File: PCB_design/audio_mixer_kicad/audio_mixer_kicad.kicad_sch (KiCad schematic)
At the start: 0 parts

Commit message: Schematics v1
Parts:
- added D1, D2: SS34, symbol Device:D_Schottky_Small
- added J1, J10, J11, J12, J13, J14, J15, J16, J17, J18, J19, J2, J20, J21, J22, J23, J24, J25, J26, J27, J28, J29, J3, J30, J31, J32, J33, J34, J35, J36, J4, J5, J6, J7, J8, J9: B3B-XH-AMLFSN, CONN_B3B-XH-AMLFSN_JST, symbol JST_XH:B3B-XH-AMLFSN
- added J37: Screw_Terminal_01x02, symbol Connector:Screw_Terminal_01x02
- added R1, R2, R3, R4, R6: 4.7k, symbol Device:R_Small_US
- added R5: 0, symbol Device:R_Small_US
- added TP1: GND, symbol Connector:TestPoint
- added TP10: D3, symbol Connector:TestPoint
- added TP11: D4, symbol Connector:TestPoint
- added TP12: D5, symbol Connector:TestPoint
- added TP13: D6, symbol Connector:TestPoint
- added TP14: D7, symbol Connector:TestPoint
- added TP15: D8, symbol Connector:TestPoint
- added TP16: D9, symbol Connector:TestPoint
- added TP17: D10, symbol Connector:TestPoint
- added TP18: D11, symbol Connector:TestPoint
- added TP19: D12, symbol Connector:TestPoint
- added TP2: 5V, symbol Connector:TestPoint
- added TP20: D13, symbol Connector:TestPoint
- added TP21: D14, symbol Connector:TestPoint
- added TP22: A15, symbol Connector:TestPoint
- added TP23: A16, symbol Connector:TestPoint
- added TP24: D17, symbol Connector:TestPoint
- added TP25: D18, symbol Connector:TestPoint
- added TP26: D19, symbol Connector:TestPoint
- added TP27: D20, symbol Connector:TestPoint
- added TP28: D21, symbol Connector:TestPoint
- added TP29: D22, symbol Connector:TestPoint
- added TP3: 3.3VD, symbol Connector:TestPoint
- added TP30: D23, symbol Connector:TestPoint
- added TP31: RST_N, symbol Connector:TestPoint
- added TP32: FPGA_CS, symbol Connector:TestPoint
- added TP33: I2C1_SDA, symbol Connector:TestPoint
- added TP34: I2C1_SCL, symbol Connector:TestPoint
- added TP35: I2C0_SDA, symbol Connector:TestPoint
- added TP36: I2C0_SCL, symbol Connector:TestPoint
- added TP37: TX, symbol Connector:TestPoint
- added TP38: D48, symbol Connector:TestPoint
- added TP39: D47, symbol Connector:TestPoint
- added TP4: 3.3VA, symbol Connector:TestPoint
- added TP40: D46, symbol Connector:TestPoint
- added TP41: D45, symbol Connector:TestPoint
- added TP42: D44, symbol Connector:TestPoint
- added TP43: D43, symbol Connector:TestPoint
- added TP44: D42, symbol Connector:TestPoint
- added TP45: D41, symbol Connector:TestPoint
- added TP46: D40, symbol Connector:TestPoint
- added TP47: D39, symbol Connector:TestPoint
- added TP48: D38, symbol Connector:TestPoint
- added TP49: D37, symbol Connector:TestPoint
- added TP5: 48V, symbol Connector:TestPoint
- added TP50: D36, symbol Connector:TestPoint
- added TP51: D35, symbol Connector:TestPoint
- added TP52: D34, symbol Connector:TestPoint
- added TP53: D33, symbol Connector:TestPoint
- added TP54: D32, symbol Connector:TestPoint
- added TP55: D31, symbol Connector:TestPoint
- added TP56: D30, symbol Connector:TestPoint
- added TP57: D29, symbol Connector:TestPoint
- added TP58: D28, symbol Connector:TestPoint
- added TP59: D27, symbol Connector:TestPoint
- added TP6: +15V, symbol Connector:TestPoint
- added TP60: D26, symbol Connector:TestPoint
- added TP61: 3V3, symbol Connector:TestPoint
- added TP62: MOSI, symbol Connector:TestPoint
- added TP63: MISO, symbol Connector:TestPoint
- added TP64: SCK, symbol Connector:TestPoint
- added TP65: RX, symbol Connector:TestPoint
- added TP66: GPO1_0, symbol Connector:TestPoint
- added TP67: GPIO1_0, symbol Connector:TestPoint
- added TP68: GPIO2_0, symbol Connector:TestPoint
- added TP69: GPO1_1, symbol Connector:TestPoint
- added TP7: -15V, symbol Connector:TestPoint
- added TP70: GPIO1_1, symbol Connector:TestPoint
- added TP71: GPIO2_1, symbol Connector:TestPoint
- added TP8: D1, symbol Connector:TestPoint
- added TP9: D2, symbol Connector:TestPoint
- added U1: XIAO-ESP32-S3-DIP, Seeed_Studio_XIAO_Series:XIAO-ESP32-S3-DIP, symbol XIAO_symbols:XIAO-ESP32-S3-DIP
- added U2: Cmod A7-35T, symbol audio_mixer_symbols:Cmod_A7-35T
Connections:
- new net: TP21.1, U2.14 (D14)
- new net: TP52.1, U2.34 (D34)
- new net: TP19.1, U2.12 (D12)
- new net: TP20.1, U2.13 (D13)
- new net: TP51.1, U2.35 (D35)
- new net: TP48.1, U2.38 (D38)
- new net: TP22.1, U2.15 (A15)
- new net: TP23.1, U2.16 (A16)
- new net: TP24.1, U2.17 (D17)
- new net: TP25.1, U2.18 (D18)
- new net: D1.1 (K), U2.24 (VU)
- new net: TP58.1, U2.28 (D28)
- new net: TP57.1, U2.29 (D29)
- new net: TP56.1, U2.30 (D30)
- new net: TP55.1, U2.31 (D31)
- new net: TP54.1, U2.32 (D32)
- new net: TP53.1, U2.33 (D33)
- new net: TP50.1, U2.36 (D36)
- new net: TP49.1, U2.37 (D37)
- new net: TP47.1, U2.39 (D39)
- new net: TP46.1, U2.40 (D40)
- new net: TP45.1, U2.41 (D41)
- new net: TP44.1, U2.42 (D42)
- new net: TP43.1, U2.43 (D43)
- new net: TP42.1, U2.44 (D44)
- new net: TP41.1, U2.45 (D45)
- new net: TP40.1, U2.46 (D46)
- new net: D2.1 (K), U1.14 (VBUS)
- new net: TP61.1, U1.12 (3V3)
- new net +15V: TP6.1
- new net +3.3V: R1.1, R2.1, R3.1, R4.1, TP3.1
- new net +3.3VA: TP4.1
- new net +48V: TP5.1
- new net +5V: D1.2 (A), D2.2 (A), TP2.1
- new net -15V: TP7.1
- new net A_PWRGATE: TP60.1, U2.26 (D26)
- new net A_PWRGATE2: TP59.1, U2.27 (D27)
- new net BCLK: TP10.1, U2.3 (D3)
- new net CH10_XLR+: J10.2
- new net CH10_XLR-: J10.3
- new net CH11_XLR+: J11.2
- new net CH11_XLR-: J11.3
- new net CH12_XLR+: J12.2
- new net CH12_XLR-: J12.3
- new net CH13_XLR+: J13.2
- new net CH13_XLR-: J13.3
- new net CH14_XLR+: J14.2
- new net CH14_XLR-: J14.3
- new net CH15_XLR+: J15.2
- new net CH15_XLR-: J15.3
- new net CH16_XLR+: J16.2
- new net CH16_XLR-: J16.3
- new net CH17_XLR+: J17.2
- new net CH17_XLR-: J17.3
- new net CH18_XLR+: J18.2
- new net CH18_XLR-: J18.3
- new net CH19_XLR+: J19.2
- new net CH19_XLR-: J19.3
- new net CH1_XLR+: J1.2
- new net CH1_XLR-: J1.3
- new net CH20_XLR+: J20.2
- new net CH20_XLR-: J20.3
- new net CH21_XLR+: J21.2
- new net CH21_XLR-: J21.3
- new net CH22_XLR+: J22.2
- new net CH22_XLR-: J22.3
- new net CH23_XLR+: J23.2
- new net CH23_XLR-: J23.3
- new net CH24_XLR+: J24.2
- new net CH24_XLR-: J24.3
- new net CH25_XLR+: J25.2
- new net CH25_XLR-: J25.3
- new net CH26_XLR+: J26.2
- new net CH26_XLR-: J26.3
- new net CH27_XLR+: J27.2
- new net CH27_XLR-: J27.3
- new net CH28_XLR+: J28.2
- new net CH28_XLR-: J28.3
- new net CH29_XLR+: J29.2
- new net CH29_XLR-: J29.3
- new net CH2_XLR+: J2.2
- new net CH2_XLR-: J2.3
- new net CH30_XLR+: J30.2
- new net CH30_XLR-: J30.3
- new net CH31_XLR+: J31.2
- new net CH31_XLR-: J31.3
- new net CH32_XLR+: J32.2
- new net CH32_XLR-: J32.3
- new net CH3_XLR+: J3.2
- new net CH3_XLR-: J3.3
- new net CH4_XLR+: J4.2
- new net CH4_XLR-: J4.3
- new net CH5_XLR+: J5.2
- new net CH5_XLR-: J5.3
- new net CH6_XLR+: J6.2
- new net CH6_XLR-: J6.3
- new net CH7_XLR+: J7.2
- new net CH7_XLR-: J7.3
- new net CH8_XLR+: J8.2
- new net CH8_XLR-: J8.3
- new net CH9_XLR+: J9.2
- new net CH9_XLR-: J9.3
- new net DAC0/ADDR: R5.1
- new net DAC0/GPIO1: TP67.1
- new net DAC0/GPIO2: TP68.1
- new net DAC0/GPO1: TP66.1
- new net DAC1/ADDR: R6.1
- new net DAC1/GPIO1: TP70.1
- new net DAC1/GPIO2: TP71.1
- new net DAC1/GPO1: TP69.1
- new net DIN0: TP38.1, U2.48 (D48)
- new net DIN1: TP39.1, U2.47 (D47)
- new net FPGA_CS: TP27.1, TP32.1, U1.2 (GPIO2_A1_D1), U2.20 (D20)
- new net FSYNC: TP9.1, U2.2 (D2)
- new net GND: J1.1, J10.1, J11.1, J12.1, J13.1, J14.1, J15.1, J16.1, J17.1, J18.1, J19.1, J2.1, J20.1, J21.1, J22.1, J23.1, J24.1, J25.1, J26.1, J27.1, J28.1, J29.1, J3.1, J30.1, J31.1, J32.1, J33.1, J34.1, J35.1, J36.1, J37.1 (Pin_1), J4.1, J5.1, J6.1, J7.1, J8.1, J9.1, R5.2, R6.2, TP1.1, U1.13 (GND), U2.25 (GND)
- new net I2C0_SCL: R4.2, TP36.1, U1.6 (GPIO6_A5_D5_SCL)
- new net I2C0_SDA: R3.2, TP35.1, U1.5 (GPIO5_A4_D4_SDA)
- new net I2C1_SCL: R2.2, TP34.1, U1.4 (GPIO4_A3_D3)
- new net I2C1_SDA: R1.2, TP33.1, U1.3 (GPIO3_A2_D2)
- new net LD0/Out+: J33.2
- new net LD0/Out-: J33.3
- new net LD1/Out+: J34.2
- new net LD1/Out-: J34.3
- new net LD2/Out+: J35.2
- new net LD2/Out-: J35.3
- new net LD3/Out+: J36.2
- new net LD3/Out-: J36.3
- new net MCLK: TP8.1, U2.1 (D1)
- new net MISO: TP29.1, TP63.1, U1.10 (GPIO8_A9_D9_MISO), U2.22 (D22)
- new net MOSI: TP28.1, TP62.1, U1.11 (GPIO9_A10_D10_MOSI), U2.21 (D21)
- new net Power/12V: J37.2 (Pin_2)
- new net RST_N: TP26.1, TP31.1, U1.1 (GPIO1_A0_D0), U2.19 (D19)
- new net RX: TP65.1, U1.8 (GPIO44_D7_RX)
- new net SCK: TP30.1, TP64.1, U1.9 (GPIO7_A8_D8_SCK), U2.23 (D23)
- new net SDOUT0: TP11.1, U2.4 (D4)
- new net SDOUT1: TP12.1, U2.5 (D5)
- new net SDOUT2: TP13.1, U2.6 (D6)
- new net SDOUT3: TP14.1, U2.7 (D7)
- new net SDOUT4: TP15.1, U2.8 (D8)
- new net SDOUT5: TP16.1, U2.9 (D9)
- new net SDOUT6: TP17.1, U2.10 (D10)
- new net SDOUT7: TP18.1, U2.11 (D11)
- new net TX: TP37.1, U1.7 (GPIO43_D6_TX)
- no-connect marks 0 -> 2
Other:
- added sheet ADC0 (adc.kicad_sch)
- added sheet ADC1 (adc.kicad_sch)
- added sheet ADC2 (adc.kicad_sch)
- added sheet ADC3 (adc.kicad_sch)
- added sheet ADC4 (adc.kicad_sch)
- added sheet ADC5 (adc.kicad_sch)
- added sheet ADC6 (adc.kicad_sch)
- added sheet ADC7 (adc.kicad_sch)
- added sheet DAC0 (dac.kicad_sch)
- added sheet DAC1 (dac.kicad_sch)
- added sheet LD0 (line_driver.kicad_sch)
- added sheet LD1 (line_driver.kicad_sch)
- added sheet LD2 (line_driver.kicad_sch)
- added sheet LD3 (line_driver.kicad_sch)
- added sheet Phantom Injector 0 (phantom_injector.kicad_sch)
- added sheet Phantom Injector 1 (phantom_injector.kicad_sch)
- added sheet Power (power.kicad_sch)
- note added: "MCU"
- note added: "Power"

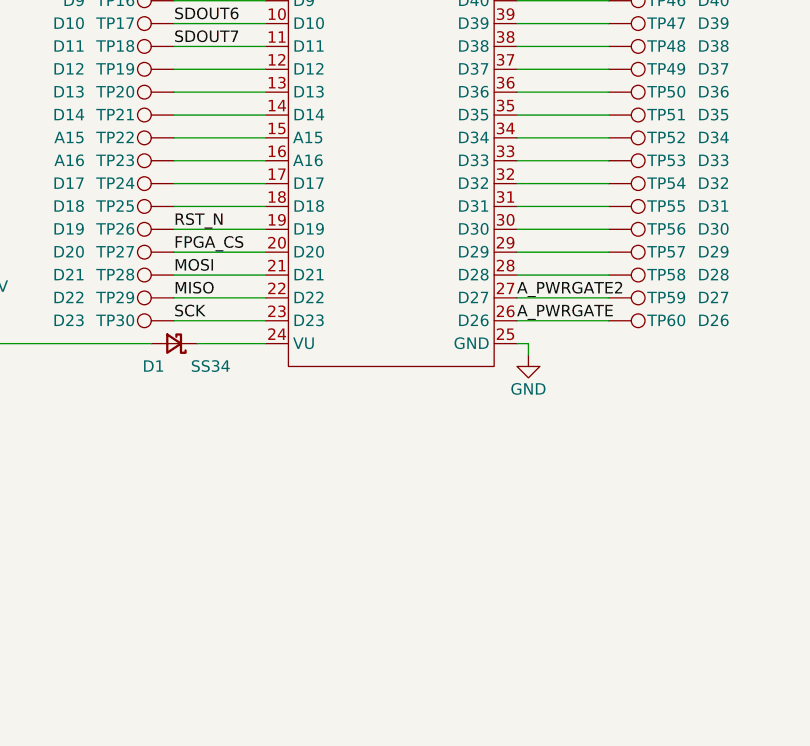
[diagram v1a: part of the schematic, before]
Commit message: Add oscillator and adc input caps
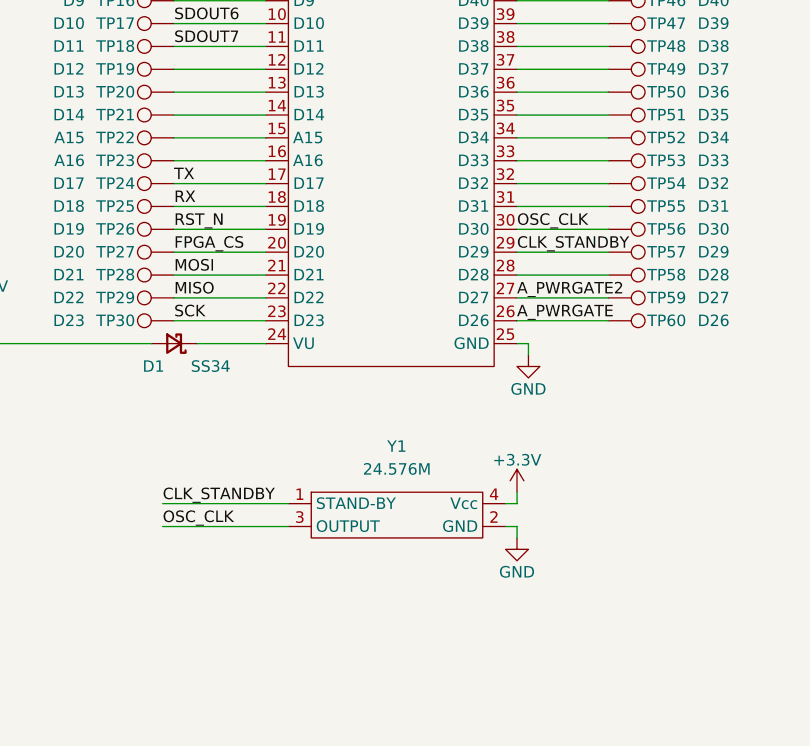
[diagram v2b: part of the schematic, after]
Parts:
- added Y1: 24.576M, symbol audio_mixer_symbols:NZ2520SDA
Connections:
- net +3.3V: now also Y1.4 (Vcc)
- net GND: now also Y1.2 (GND)
- net RX: now also TP25.1, U2.18 (D18)
- net TX: now also TP24.1, U2.17 (D17)
- net CLK_STANDBY: now reaches TP57.1, U2.29 (D29)
- net CLK_STANDBY: now also Y1.1 (STAND-BY)
- net OSC_CLK: now reaches TP56.1, U2.30 (D30)
- net OSC_CLK: now also Y1.3 (OUTPUT)

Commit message: Reannotate and add passives for Y1
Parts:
- added C1: 0.1u, symbol Device:C_Small
- added R5: 22, symbol Device:R_Small_US
- added R6: 10k, symbol Device:R_Small_US
- renumbered J37 to J33, J33 to J34, J34 to J35, J35 to J36, J36 to J37, R5 to R7, R6 to R8
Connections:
- net +3.3V: now also C1.1, R6.1
- net CLK_STANDBY: now also R6.2
- net GND: now also C1.2
- net OSC_CLK: now also R5.1; no longer Y1.3 (OUTPUT)
- new net: R5.2, Y1.3 (OUTPUT)

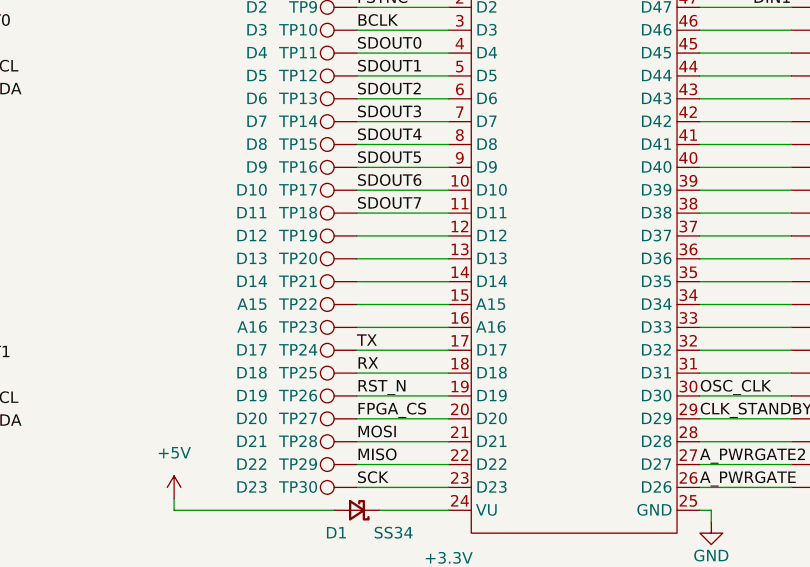
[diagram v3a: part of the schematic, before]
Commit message: Route I2C to FPGA
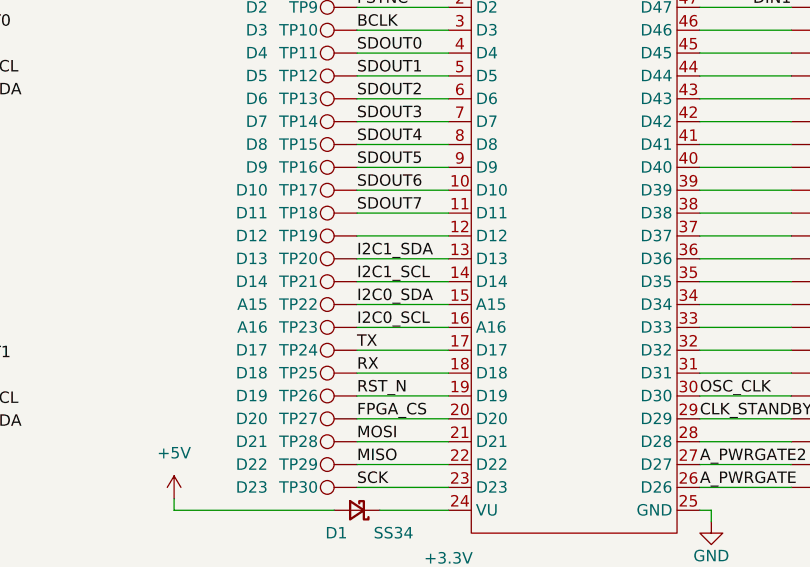
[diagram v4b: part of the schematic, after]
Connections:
- net I2C0_SCL: now also TP23.1, U2.16 (A16)
- net I2C0_SDA: now also TP22.1, U2.15 (A15)
- net I2C1_SCL: now also TP21.1, U2.14 (D14)
- net I2C1_SDA: now also TP20.1, U2.13 (D13)
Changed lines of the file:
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@@
+		)
+	)
+	(label "I2C0_SCL"
+		(at 153.67 100.33 0)
+		(effects
+			(font
+				(size 1.27 1.27)
+			)
+			(justify left bottom)
 		)
 	)
@@
 		)
 	)
+	(label "I2C0_SDA"
+		(at 153.67 97.79 0)
+		(effects
+			(font
+				(size 1.27 1.27)
+			)
+			(justify left bottom)
+		)
+	)
 	(label "CH29_ADC-"
 		(at 66.04 321.31 0)
@@
 		)
 	)
+	(label "I2C1_SCL"
+		(at 153.67 95.25 0)
+		(effects
+			(font
+				(size 1.27 1.27)
+			)
+			(justify left bottom)
+		)
+	)
 	(label "CH30_XLR+"
 		(at 0 251.46 0)
@@
 		)
 	)
+	(label "I2C1_SDA"
+		(at 153.67 92.71 0)
+		(effects
+			(font
+				(size 1.27 1.27)
+			)
+			(justify left bottom)
+		)
+	)

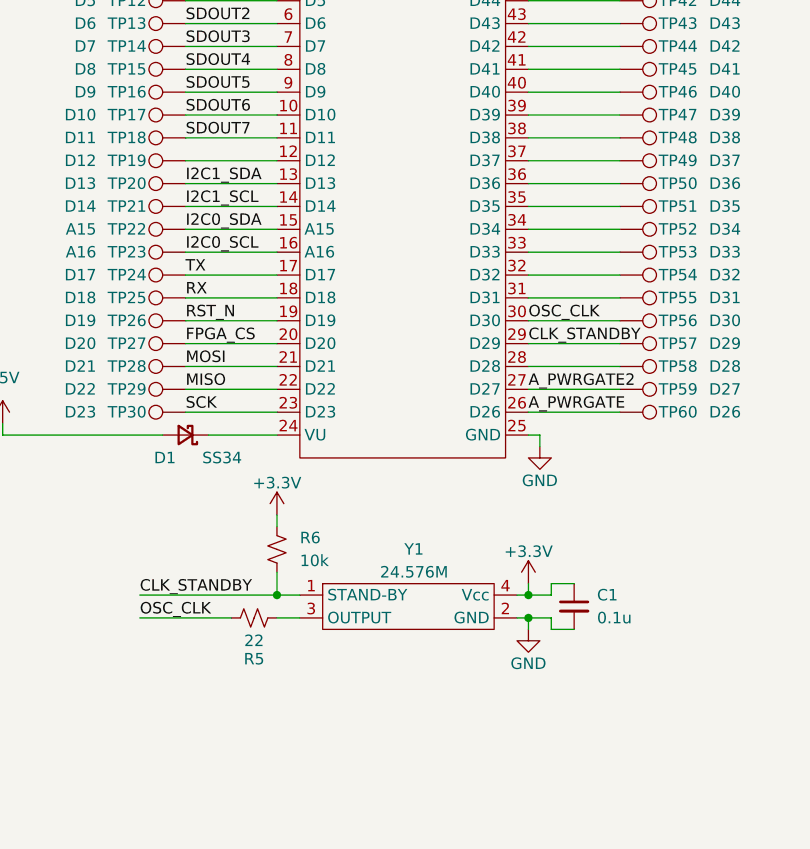
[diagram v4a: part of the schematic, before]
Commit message: Move I2C pins away from FPGA analog ports
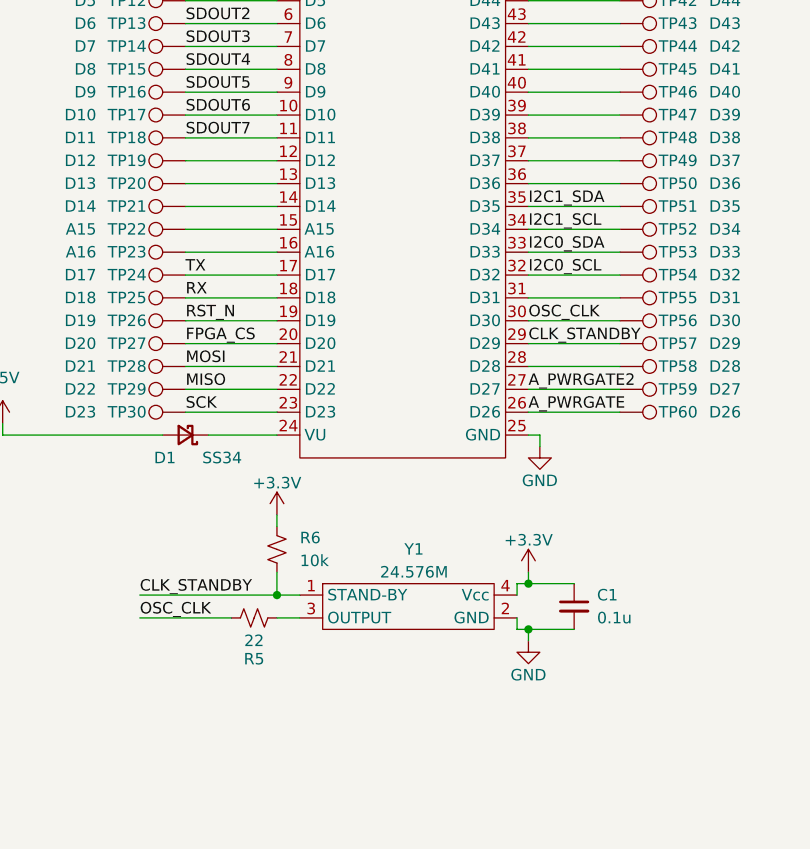
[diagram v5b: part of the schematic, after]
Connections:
- net I2C0_SCL: now also TP54.1, U2.32 (D32); no longer TP23.1, U2.16 (A16)
- net I2C0_SDA: now also TP53.1, U2.33 (D33); no longer TP22.1, U2.15 (A15)
- net I2C1_SCL: now also TP52.1, U2.34 (D34); no longer TP21.1, U2.14 (D14)
- net I2C1_SDA: now also TP51.1, U2.35 (D35); no longer TP20.1, U2.13 (D13)
- new net: TP21.1, U2.14 (D14)
- new net: TP20.1, U2.13 (D13)
- new net: TP22.1, U2.15 (A15)
- new net: TP23.1, U2.16 (A16)
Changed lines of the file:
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@@
 	)
 	(junction
-		(at 191.77 138.43)
+		(at 95.25 31.75)
 		(diameter 0)
 		(color 0 0 0 0)
 	)
 	(junction
-		(at 95.25 31.75)
+		(at 90.17 29.21)
 		(diameter 0)
 		(color 0 0 0 0)
 	)
 	(junction
-		(at 90.17 29.21)
+		(at 107.95 232.41)
 		(diameter 0)
 		(color 0 0 0 0)
 	)
 	(junction
-		(at 107.95 232.41)
+		(at 191.77 142.24)
 		(diameter 0)
 		(color 0 0 0 0)
@@
 	)
 	(junction
-		(at 191.77 140.97)
+		(at 191.77 137.16)
 		(diameter 0)
 		(color 0 0 0 0)
@@
 	(wire
 		(pts
-			(xy 196.85 142.24) (xy 194.31 142.24)
-		)
-		(stroke
-			(width 0)
-			(type default)
-		)
-	)
-	(wire
-		(pts
 			(xy 107.95 270.51) (xy 107.95 269.24)
 		)
@@
 	(wire
 		(pts
+			(xy 190.5 142.24) (xy 190.5 140.97)
+		)
+		(stroke
+			(width 0)
+			(type default)
+		)
+	)
+	(wire
+		(pts
 			(xy 257.81 74.93) (xy 267.97 74.93)
 		)
@@
 	(wire
 		(pts
-			(xy 191.77 137.16) (xy 191.77 138.43)
+			(xy 191.77 135.89) (xy 191.77 137.16)
 		)
 		(stroke
@@
 	(wire
 		(pts
-			(xy 196.85 137.16) (xy 194.31 137.16)
-		)
-		(stroke
-			(width 0)
-			(type default)
-		)
-	)
-	(wire
-		(pts
 			(xy 0 256.54) (xy 11.43 256.54)
 		)
@@
 	(wire
 		(pts
-			(xy 191.77 138.43) (xy 190.5 138.43)
+			(xy 191.77 137.16) (xy 190.5 137.16)
 		)
 		(stroke
@@
 	(wire
 		(pts
-			(xy 194.31 138.43) (xy 191.77 138.43)
+			(xy 191.77 137.16) (xy 196.85 137.16)
 		)
 		(stroke
@@
 	(wire
 		(pts
+			(xy 191.77 143.51) (xy 191.77 142.24)
+		)
+		(stroke
+			(width 0)
+			(type default)
+		)
+	)
+	(wire
+		(pts
 			(xy 48.26 151.13) (xy 50.8 151.13)
 		)
@@
 	(wire
 		(pts
-			(xy 194.31 137.16) (xy 194.31 138.43)
-		)
-		(stroke
-			(width 0)
-			(type default)
-		)
-	)
-	(wire
-		(pts
 			(xy -46.99 224.79) (xy -35.56 224.79)
 		)
@@
 	(wire
 		(pts
-			(xy 194.31 142.24) (xy 194.31 140.97)
-		)
-		(stroke
-			(width 0)
-			(type default)
-		)
-	)
-	(wire
-		(pts
 			(xy 105.41 229.87) (xy 107.95 229.87)
 		)
@@
 	(wire
 		(pts
-			(xy 194.31 140.97) (xy 191.77 140.97)
+			(xy 191.77 142.24) (xy 196.85 142.24)
 		)
 		(stroke
@@
 	(wire
 		(pts
-			(xy 48.26 133.35) (xy 59.69 133.35)
+			(xy 190.5 137.16) (xy 190.5 138.43)
 		)
 		(stroke
@@
 	(wire
 		(pts
-			(xy 334.01 111.76) (xy 323.85 111.76)
+			(xy 48.26 133.35) (xy 59.69 133.35)
 		)
 		(stroke
@@
 	(wire
 		(pts
-			(xy -45.72 173.99) (xy -45.72 175.26)
+			(xy 334.01 111.76) (xy 323.85 111.76)
 		)
 		(stroke
@@
 	(wire
 		(pts
-			(xy 191.77 100.33) (xy 201.93 100.33)
+			(xy -45.72 173.99) (xy -45.72 175.26)
 		)
 		(stroke
@@
 	(wire
 		(pts
-			(xy 66.04 218.44) (xy 77.47 218.44)
+			(xy 191.77 100.33) (xy 201.93 100.33)
 		)
 		(stroke
@@
 	(wire
 		(pts
-			(xy 87.63 314.96) (xy 87.63 316.23)
+			(xy 66.04 218.44) (xy 77.47 218.44)
 		)
 		(stroke
@@
 	(wire
 		(pts
-			(xy 191.77 140.97) (xy 191.77 142.24)
+			(xy 87.63 314.96) (xy 87.63 316.23)
 		)
 		(stroke
@@
 	(wire
 		(pts
-			(xy 190.5 140.97) (xy 191.77 140.97)
+			(xy 190.5 142.24) (xy 191.77 142.24)
 		)
 		(stroke
@@
 		)
 	)
-	(label "I2C0_SCL"
-		(at 153.67 100.33 0)
-		(effects
-			(font
-				(size 1.27 1.27)
-			)
-			(justify left bottom)
-		)
-	)
 	(label "FSYNC"
 		(at 107.95 99.06 0)
@@
 		)
 	)
-	(label "I2C0_SDA"
-		(at 153.67 97.79 0)
-		(effects
-			(font
-				(size 1.27 1.27)
-			)
-			(justify left bottom)
-		)
-	)
 	(label "CH29_ADC-"
 		(at 66.04 321.31 0)
@@
 		)
 	)
-	(label "I2C1_SCL"
-		(at 153.67 95.25 0)
-		(effects
-			(font
-				(size 1.27 1.27)
-			)
-			(justify left bottom)
-		)
-	)
 	(label "CH30_XLR+"
 		(at 0 251.46 0)
@@
 		)
 	)
-	(label "I2C1_SDA"
-		(at 153.67 92.71 0)
-		(effects
-			(font
-				(size 1.27 1.27)
-			)
-			(justify left bottom)
-		)
-	)
 	(label "MCLK"
 		(at 257.81 107.95 0)
@@
 		)
 	)
+	(label "I2C1_SCL"
+		(at 191.77 97.79 0)
+		(effects
+			(font
+				(size 1.27 1.27)
+			)
+			(justify left bottom)
+		)
+	)
 	(label "CH14_XLR-"
 		(at -74.93 293.37 180)
@@
 		)
 	)
+	(label "I2C0_SCL"
+		(at 191.77 102.87 0)
+		(effects
+			(font
+				(size 1.27 1.27)
+			)
+			(justify left bottom)
+		)
+	)
 	(label "I2C1_SDA"
 		(at 107.95 295.91 0)
@@
 		)
 	)
+	(label "I2C1_SDA"
+		(at 191.77 95.25 0)
+		(effects
+			(font
+				(size 1.27 1.27)
+			)
+			(justify left bottom)
+		)
+	)
 	(label "CH20_ADC-"
 		(at 66.04 226.06 0)
@@
 		)
 	)
+	(label "I2C0_SDA"
+		(at 191.77 100.33 0)
+		(effects
+			(font
+				(size 1.27 1.27)
+			)
+			(justify left bottom)
+		)
+	)
 	(label "CH9_ADC-"
 		(at 59.69 110.49 180)
@@
 	(symbol
 		(lib_id "power:GND")
-		(at 191.77 142.24 0)
+		(at 191.77 143.51 0)
 		(unit 1)
 		(body_style 1)
@@
 		(dnp no)
 		(property "Reference" "#PWR093"
-			(at 191.77 148.59 0)
+			(at 191.77 149.86 0)
 			(hide yes)
 			(show_name no)
@@
 		)
 		(property "Value" "GND"
-			(at 191.77 146.05 0)
+			(at 191.77 147.32 0)
 			(show_name no)
 			(do_not_autoplace no)
@@
 		)
 		(property "Footprint" ""
-			(at 191.77 142.24 0)
+			(at 191.77 143.51 0)
 			(hide yes)
 			(show_name no)
@@
 		)
 		(property "Datasheet" ""
-			(at 191.77 142.24 0)
+			(at 191.77 143.51 0)
 			(hide yes)
 			(show_name no)
@@
 		)
 		(property "Description" "Power symbol creates a global label with name \"GND\" , ground"
-			(at 191.77 142.24 0)
+			(at 191.77 143.51 0)
 			(hide yes)
 			(show_name no)
@@
 	(symbol
 		(lib_id "power:+3.3V")
-		(at 191.77 137.16 0)
+		(at 191.77 135.89 0)
 		(unit 1)
 		(body_style 1)
@@
 		(dnp no)
 		(property "Reference" "#PWR092"
-			(at 191.77 140.97 0)
+			(at 191.77 139.7 0)
 			(hide yes)
 			(show_name no)
@@
 		)
 		(property "Value" "+3.3V"
-			(at 191.77 133.604 0)
+			(at 191.77 132.334 0)
 			(show_name no)
 			(do_not_autoplace no)
@@
 		)
 		(property "Footprint" ""
-			(at 191.77 137.16 0)
+			(at 191.77 135.89 0)
 			(hide yes)
 			(show_name no)
@@
 		)
 		(property "Datasheet" ""
-			(at 191.77 137.16 0)
+			(at 191.77 135.89 0)
 			(hide yes)
 			(show_name no)
@@
 		)
 		(property "Description" "Power symbol creates a global label with name \"+3.3V\""
-			(at 191.77 137.16 0)
+			(at 191.77 135.89 0)
 			(hide yes)
 			(show_name no)
